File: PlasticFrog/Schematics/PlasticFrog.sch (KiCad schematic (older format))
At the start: 8 parts, among them J1 USB_A, J2 Conn_01x04, J3 Conn_01x05, U1 CH552T

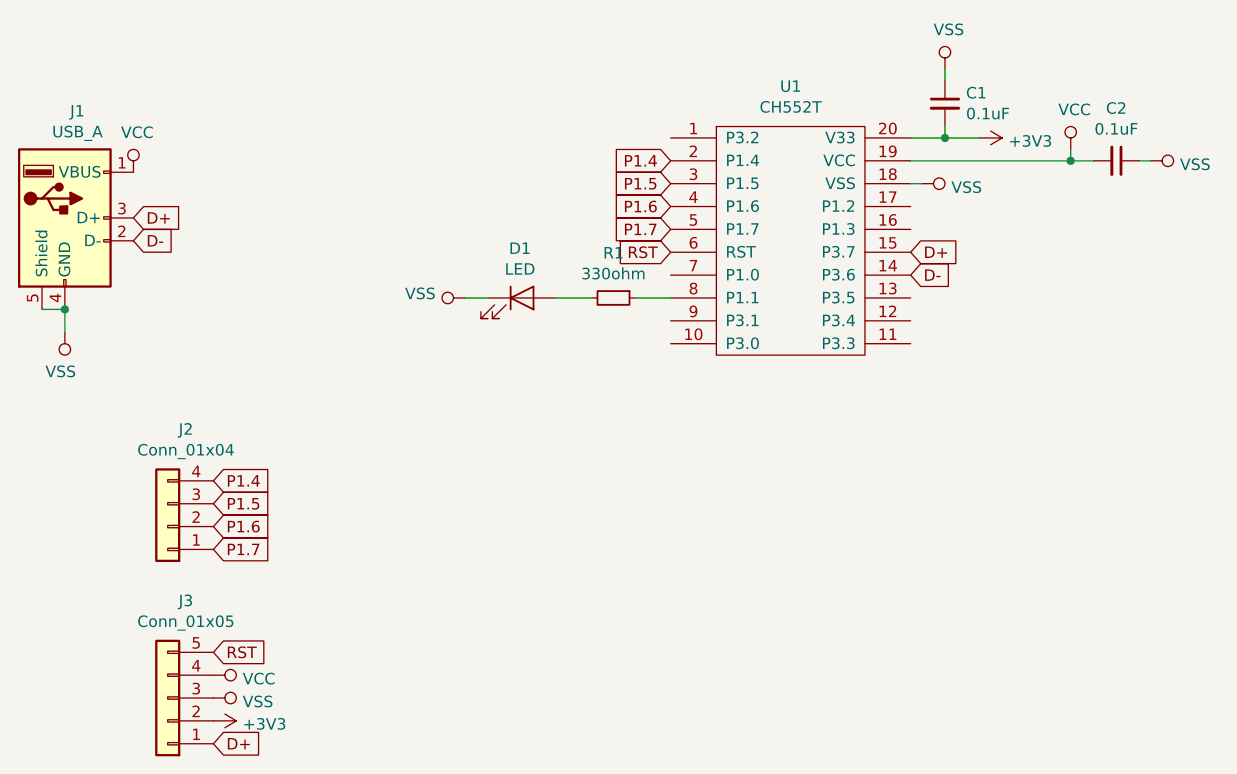
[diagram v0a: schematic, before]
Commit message: Cant believe I had D+ and D- mixed...
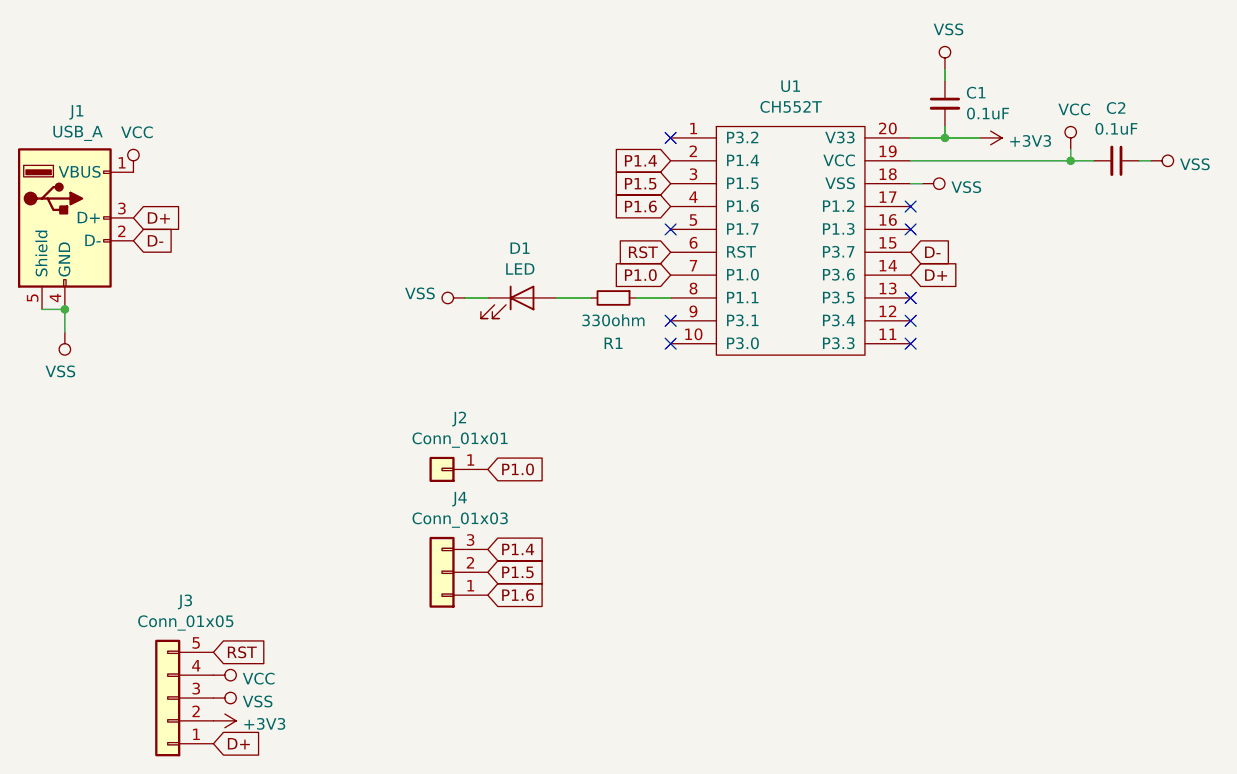
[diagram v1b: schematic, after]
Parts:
- removed J2: Conn_01x04, Pin_Headers:Pin_Header_Straight_1x04_Pitch2.54mm, symbol Connector_Generic:Conn_01x04
- added J2: Conn_01x01, Card:TouchPad_small, symbol Connector_Generic:Conn_01x01
- added J4: Conn_01x03, Pin_Headers:Pin_Header_Straight_1x03_Pitch2.54mm, symbol Connector_Generic:Conn_01x03
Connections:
- net D+: now also U1.14 (P3.6); no longer U1.15 (P3.7)
- net D-: now also U1.15 (P3.7); no longer U1.14 (P3.6)
- net P1.4: now also J4.3 (Pin_3)
- net P1.5: now also J4.2 (Pin_2)
- net P1.6: now also J4.1 (Pin_1)
- net P1.0: now reaches U1.7 (P1.0)
- net P1.0: now also J2.1 (Pin_1)
- net P1.7: no longer names the net of U1.5 (P1.7)
- no-connect marks 0 -> 9
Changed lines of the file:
@@
 LIBS:power
 LIBS:74xx
+LIBS:PlasticFrog-cache
 EELAYER 26 0
 EELAYER END
@@
 Text GLabel 3650 2450 2    50   Input ~ 0
 D-
+Text GLabel 7050 2600 2    50   Input ~ 0
+D+
 Text GLabel 7050 2500 2    50   Input ~ 0
-D+
-Text GLabel 7050 2600 2    50   Input ~ 0
 D-
 $Comp
@@
 U 1 1 5C809640
 P 5750 2700
-F 0 "R1" V 5554 2700 50  0000 C CNN
-F 1 "330ohm" V 5645 2700 50  0000 C CNN
+F 0 "R1" V 5950 2700 50  0000 C CNN
+F 1 "330ohm" V 5850 2700 50  0000 C CNN
 F 2 "Resistors_SMD:R_0805" H 5750 2700 50  0001 C CNN
 F 3 "~" H 5750 2700 50  0001 C CNN
@@
 Wire Wire Line
 	7750 2100 7850 2100
-$Comp
-L Connector_Generic:Conn_01x04 J2
-U 1 1 5C809E26
-P 3800 3700
-F 0 "J2" H 3720 3275 50  0000 C CNN
-F 1 "Conn_01x04" H 3720 3366 50  0000 C CNN
-F 2 "Pin_Headers:Pin_Header_Straight_1x04_Pitch2.54mm" H 3800 3700 50  0001 C CNN
-F 3 "~" H 3800 3700 50  0001 C CNN
-	1    3800 3700
-	-1   0    0    1
-$EndComp
 Text GLabel 6000 2500 0    50   Input ~ 0
 RST
@@
 Text GLabel 4000 4650 2    50   Input ~ 0
 D+
-Text GLabel 4000 3500 2    50   Input ~ 0
+Text GLabel 5200 3800 2    50   Input ~ 0
 P1.4
-Text GLabel 4000 3600 2    50   Input ~ 0
+Text GLabel 5200 3900 2    50   Input ~ 0
 P1.5
-Text GLabel 4000 3700 2    50   Input ~ 0
+Text GLabel 5200 4000 2    50   Input ~ 0
 P1.6
-Text GLabel 4000 3800 2    50   Input ~ 0
-P1.7
+Text GLabel 5200 3450 2    50   Input ~ 0
+P1.0
 Text GLabel 6000 2100 0    50   Input ~ 0
 P1.4
@@
 Text GLabel 6000 2300 0    50   Input ~ 0
 P1.6
-Text GLabel 6000 2400 0    50   Input ~ 0
-P1.7
+Text GLabel 6000 2600 0    50   Input ~ 0
+P1.0
 $Comp
 L power:VSS #PWR0111
@@
 Wire Wire Line
 	7050 2200 7100 2200
+NoConn ~ 6000 2000
+NoConn ~ 6000 2800
+NoConn ~ 6000 2900
+NoConn ~ 7050 2900
+NoConn ~ 7050 2800
+NoConn ~ 7050 2700
+NoConn ~ 7050 2400
+NoConn ~ 7050 2300
+NoConn ~ 6000 2400
+$Comp
+L Connector_Generic:Conn_01x01 J2
+U 1 1 5C98599F
+P 5000 3450
+F 0 "J2" H 4920 3225 50  0000 C CNN
+F 1 "Conn_01x01" H 4920 3316 50  0000 C CNN
+F 2 "Card:TouchPad_small" H 5000 3450 50  0001 C CNN
+F 3 "~" H 5000 3450 50  0001 C CNN
+	1    5000 3450
+	-1   0    0    1
+$EndComp
+$Comp
+L Connector_Generic:Conn_01x03 J4
+U 1 1 5C985AF2
+P 5000 3900
+F 0 "J4" H 4920 3575 50  0000 C CNN
+F 1 "Conn_01x03" H 4920 3666 50  0000 C CNN
+F 2 "Pin_Headers:Pin_Header_Straight_1x03_Pitch2.54mm" H 5000 3900 50  0001 C CNN
+F 3 "~" H 5000 3900 50  0001 C CNN
+	1    5000 3900
+	-1   0    0    1
+$EndComp
 $EndSCHEMATC
